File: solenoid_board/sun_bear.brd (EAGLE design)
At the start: 38.1 x 38.1 mm, 31 parts, among them Q1 MOSFET-NCHANNELSMD, Q2 MOSFET-NCHANNELSMD, Q3 MOSFET-NCHANNELSMD, Q4 MOSFET-NCHANNELSMD

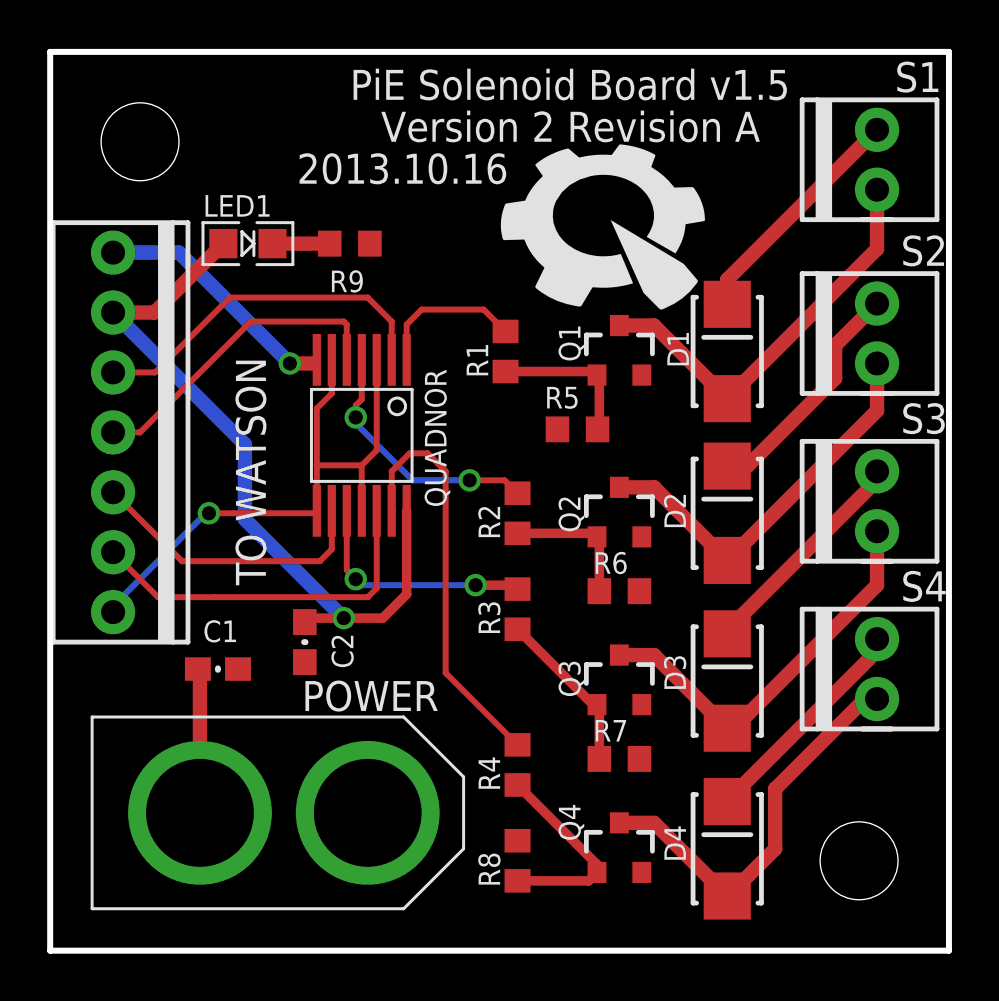
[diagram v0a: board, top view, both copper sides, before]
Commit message: Fixed Right Angle Traces on Sunbear
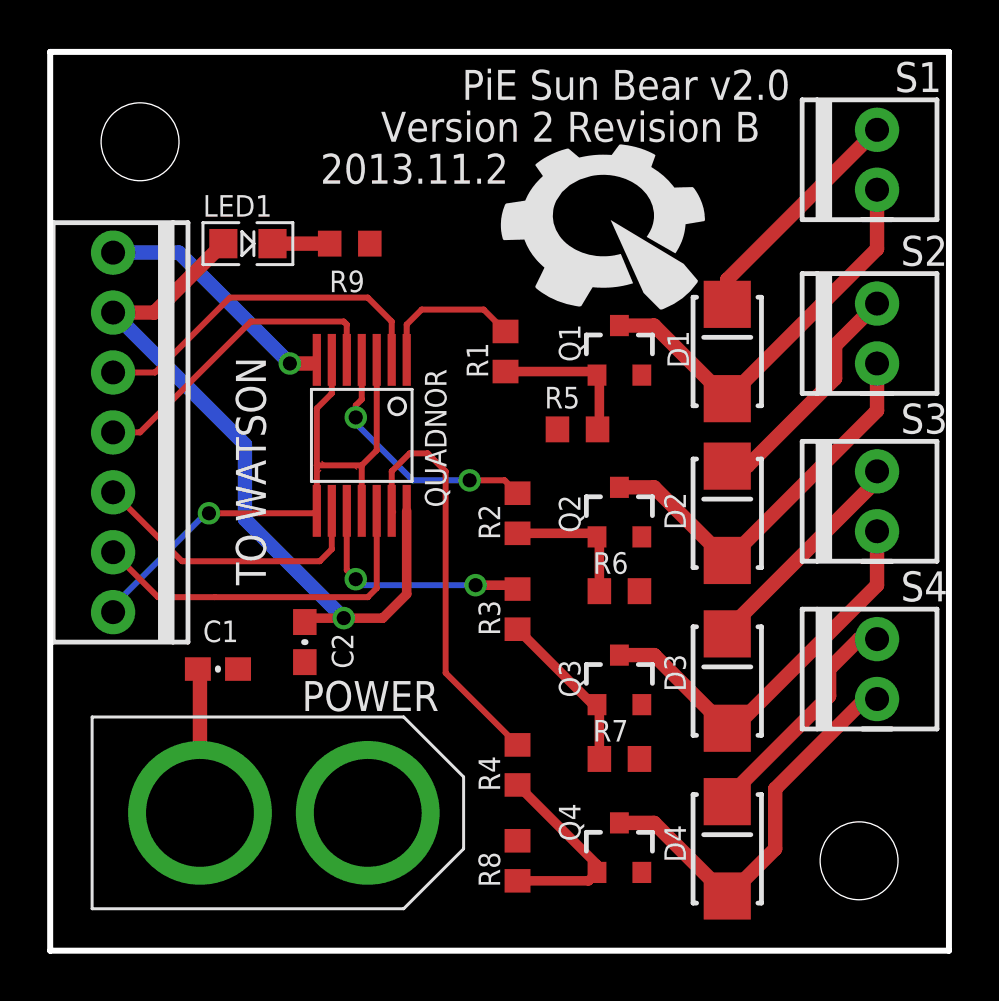
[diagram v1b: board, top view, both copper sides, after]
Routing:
- added copper zone on layer 1, net IO61
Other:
- board text added: "2013.11.2"
- board text added: "PiE Sun Bear v2.0"
- board text added: "Version 2 Revision B"
- board text removed: "2013.10.16"
- board text removed: "PiE Solenoid Board v1.5"
- board text removed: "Version 2 Revision A"
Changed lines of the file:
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@@
 <wire x1="38.1" y1="38.1" x2="0" y2="38.1" width="0.254" layer="20"/>
 <wire x1="0" y1="38.1" x2="0" y2="0" width="0.254" layer="20"/>
-<text x="31.369" y="37.338" size="1.27" layer="25" font="vector" ratio="20" rot="R180">PiE Solenoid Board v1.5</text>
-<text x="30.099" y="35.56" size="1.27" layer="21" font="vector" ratio="20" rot="R180">Version 2 Revision A</text>
-<text x="19.431" y="33.782" size="1.27" layer="21" font="vector" ratio="20" rot="R180">2013.10.16</text>
+<text x="31.369" y="37.338" size="1.27" layer="25" font="vector" ratio="20" rot="R180">PiE Sun Bear v2.0</text>
+<text x="30.099" y="35.56" size="1.27" layer="21" font="vector" ratio="20" rot="R180">Version 2 Revision B</text>
+<text x="19.431" y="33.782" size="1.27" layer="21" font="vector" ratio="20" rot="R180">2013.11.2</text>
 <text x="10.668" y="10.16" size="1.27" layer="21" font="vector" ratio="20">POWER</text>
 <text x="9.144" y="15.494" size="1.27" layer="21" font="vector" ratio="20" rot="SR90">TO WATSON</text>
@@
 <wire x1="34.798" y1="19.685" x2="34.798" y2="20.066" width="0.6096" layer="1"/>
 <wire x1="34.798" y1="20.066" x2="35.052" y2="20.32" width="0.6096" layer="1"/>
-<wire x1="28.702" y1="6.318" x2="28.702" y2="6.35" width="0.6096" layer="1"/>
-<wire x1="28.702" y1="6.35" x2="35.052" y2="12.7" width="0.6096" layer="1"/>
-<wire x1="35.052" y1="12.7" x2="35.052" y2="13.208" width="0.6096" layer="1"/>
-<wire x1="33.274" y1="25.654" x2="28.702" y2="27.4" width="0" layer="19" extent="1-1"/>
-<wire x1="35.052" y1="20.32" x2="33.274" y2="24.257" width="0" layer="19" extent="1-1"/>
-<wire x1="35.052" y1="13.208" x2="28.702" y2="13.43" width="0" layer="19" extent="1-1"/>
-<wire x1="6.35" y1="5.842" x2="28.702" y2="6.318" width="0" layer="19" extent="1-1"/>
+<wire x1="28.702" y1="6.318" x2="28.702" y2="6.477" width="0.6096" layer="1"/>
+<wire x1="28.702" y1="6.477" x2="33.02" y2="10.795" width="0.6096" layer="1"/>
+<wire x1="33.02" y1="10.795" x2="33.02" y2="11.938" width="0.6096" layer="1"/>
+<wire x1="33.02" y1="11.938" x2="34.29" y2="13.208" width="0.6096" layer="1"/>
+<wire x1="34.29" y1="13.208" x2="35.052" y2="13.208" width="0.6096" layer="1"/>
 </signal>
 <signal name="N$15">
@@
 <wire x1="11.303" y1="20.574" x2="11.303" y2="18.644" width="0.254" layer="1"/>
 <wire x1="11.938" y1="25.044" x2="11.938" y2="23.622" width="0.254" layer="1"/>
-<wire x1="13.208" y1="20.574" x2="11.303" y2="20.574" width="0.254" layer="1"/>
-<wire x1="13.208" y1="20.574" x2="13.843" y2="21.209" width="0.254" layer="1"/>
 <wire x1="13.843" y1="21.209" x2="13.843" y2="25.044" width="0.254" layer="1"/>
 <contactref element="WATSON" pad="7"/>
 <wire x1="6.604" y1="18.542" x2="2.667" y2="14.605" width="0.254" layer="16"/>
 <wire x1="2.667" y1="14.605" x2="2.667" y2="14.351" width="0.254" layer="16"/>
+<wire x1="13.208" y1="20.574" x2="13.843" y2="21.209" width="0.254" layer="1"/>
+<wire x1="11.303" y1="20.574" x2="13.208" y2="20.574" width="0.254" layer="1"/>
+<polygon width="0.254" layer="1">
+<vertex x="13.208" y="20.574"/>
+<vertex x="12.827" y="20.574"/>
+<vertex x="13.208" y="20.193"/>
+</polygon>
+<polygon width="0.254" layer="1">
+<vertex x="11.303" y="20.193"/>
+<vertex x="11.684" y="20.574"/>
+<vertex x="11.303" y="20.955"/>
+</polygon>
 </signal>
 <signal name="VCC" class="1">
@@
 </signal>
 </signals>
+<errors>
+</errors>
 </board>
 </drawing>

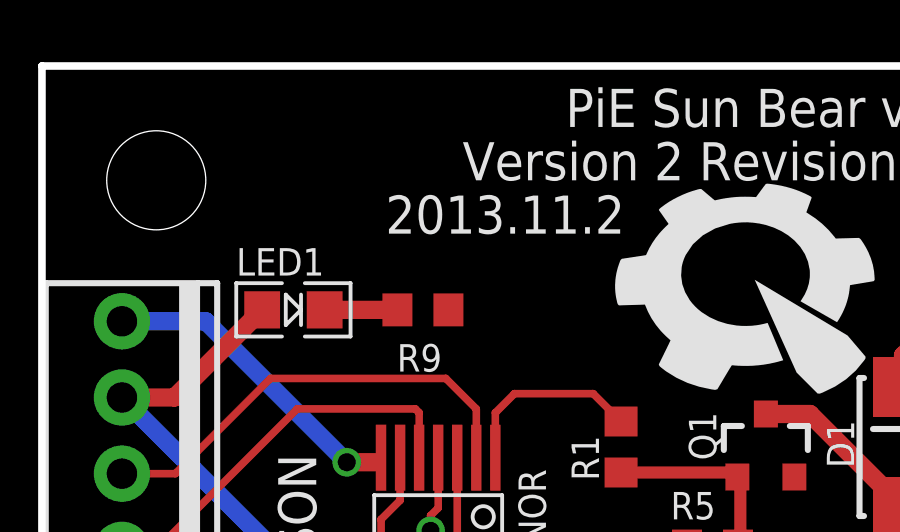
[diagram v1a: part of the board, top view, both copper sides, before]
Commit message: Silkscreen date changed to 11/11
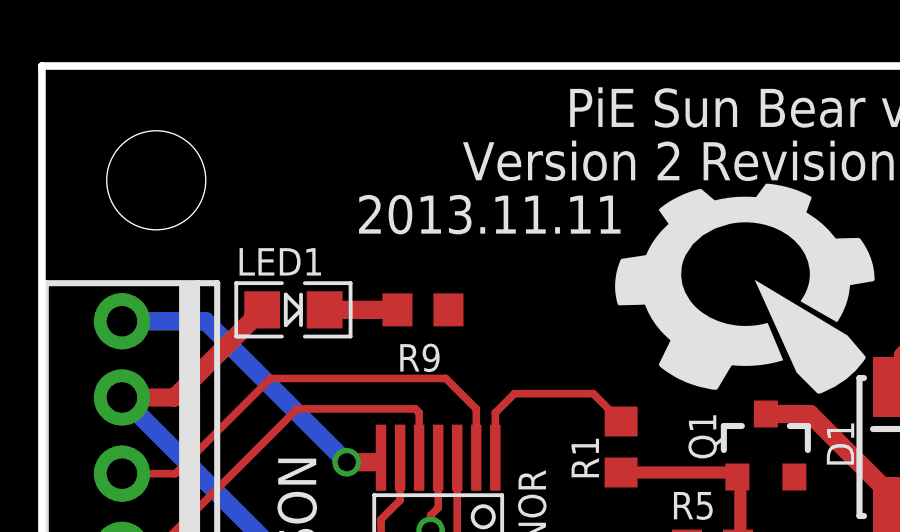
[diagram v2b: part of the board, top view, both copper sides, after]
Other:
- board text added: "2013.11.11"
- board text removed: "2013.11.2"
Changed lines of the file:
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@@
 <text x="31.369" y="37.338" size="1.27" layer="25" font="vector" ratio="20" rot="R180">PiE Sun Bear v2.0</text>
 <text x="30.099" y="35.56" size="1.27" layer="21" font="vector" ratio="20" rot="R180">Version 2 Revision B</text>
-<text x="19.431" y="33.782" size="1.27" layer="21" font="vector" ratio="20" rot="R180">2013.11.2</text>
+<text x="19.431" y="33.782" size="1.27" layer="21" font="vector" ratio="20" rot="R180">2013.11.11</text>
 <text x="10.668" y="10.16" size="1.27" layer="21" font="vector" ratio="20">POWER</text>
 <text x="9.144" y="15.494" size="1.27" layer="21" font="vector" ratio="20" rot="SR90">TO WATSON</text>

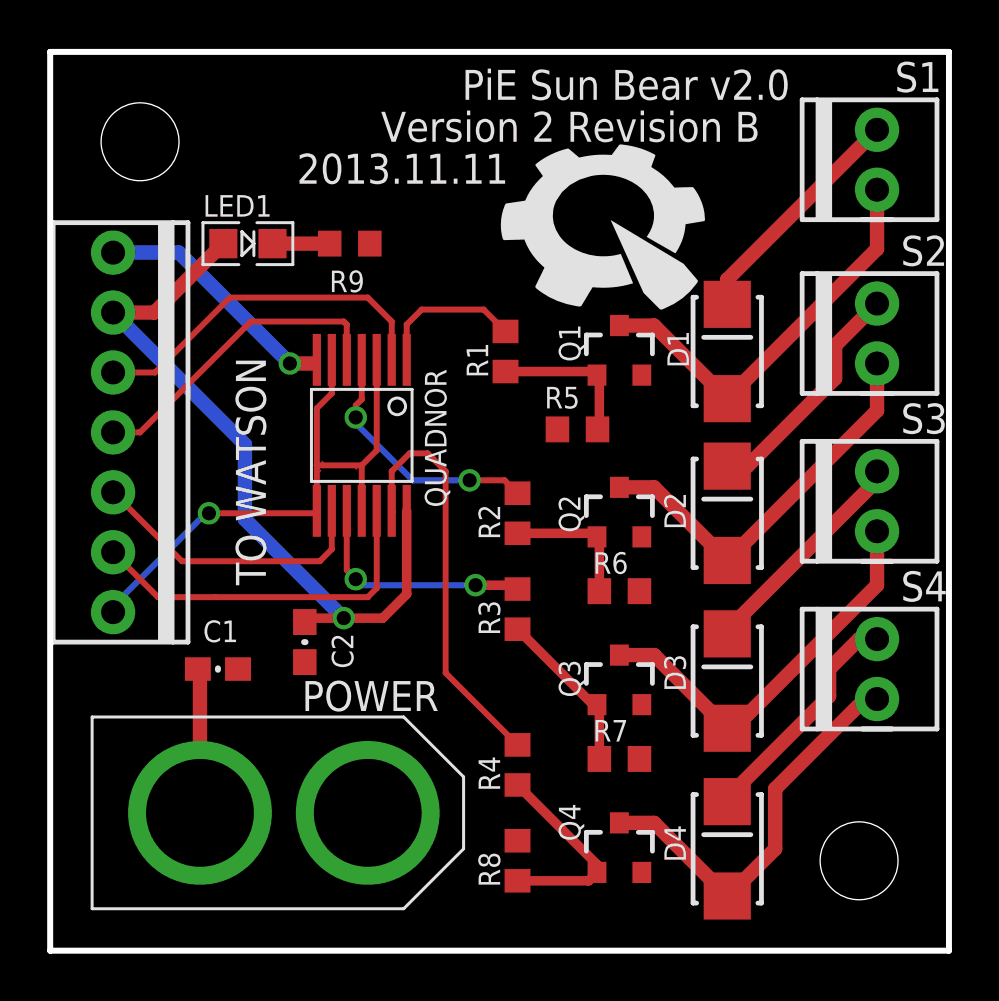
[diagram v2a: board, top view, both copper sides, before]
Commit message: Moved connectors, added screw hole for enclosure
Moved the XT60 and M70 a little bit down to give the connectors some
extra clearance, added a third screw hole to get three points of
contact, moved the silkscreen PiE logo a bit.
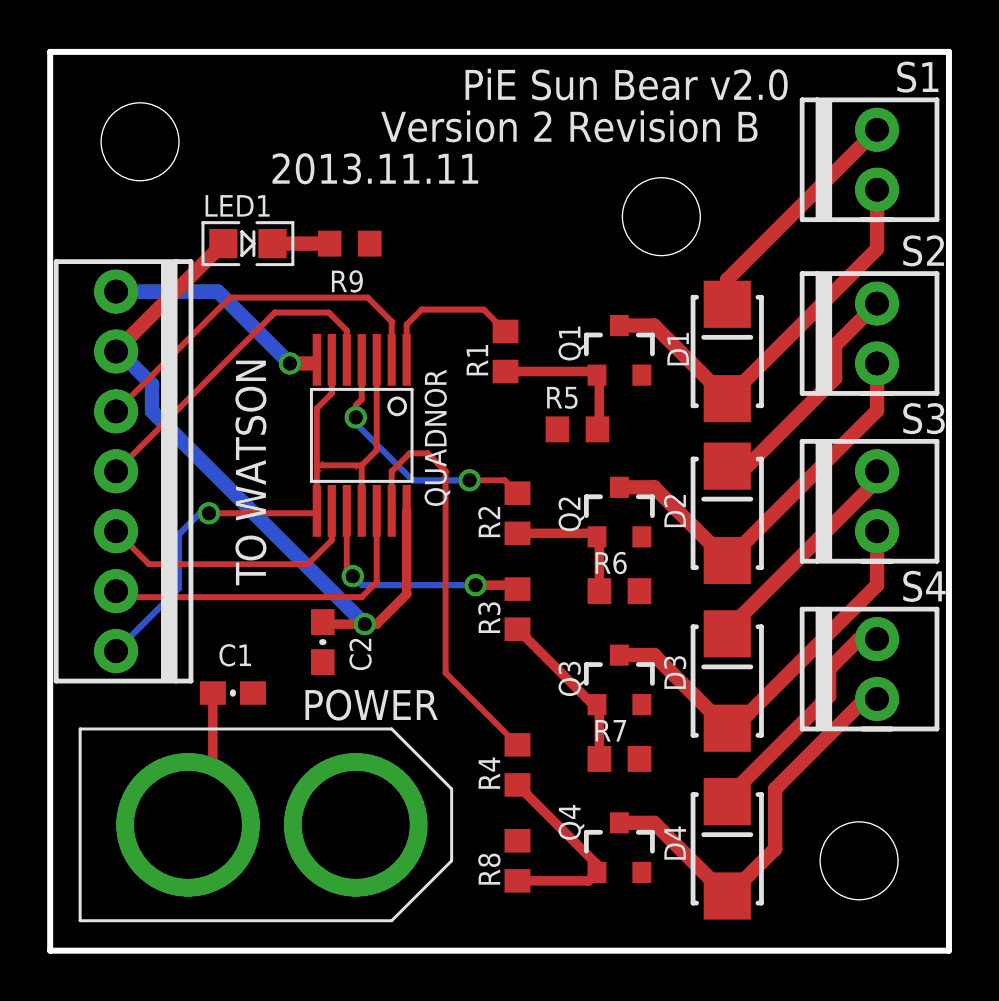
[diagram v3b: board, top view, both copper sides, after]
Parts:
- added U$6: Mounting + Test, pie:STAND-OFF
- moved U$1 26.3 mm to (27.3, 4.95), flipped to the bottom
- moved WATSON 1.66 mm to (2.79, 20.3)
- moved C1 1.20 mm to (7.75, 10.9)
- moved C2 0.76 mm to (11.6, 13.1)
- moved U$2 0.72 mm to (9.40, 5.33)
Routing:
- net IO61: track 25.8 -> 27.5 mm
- net VCC: track 31.2 -> 30.1 mm
- net IO65: track 15.4 -> 14.4 mm
- net IO21: track 12.3 -> 11.4 mm
- net GND: track 10.6 -> 9.83 mm
- net IO63: track 13.4 -> 14.1 mm
- net IO64: track 15.2 -> 15.7 mm
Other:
- board text added: "Copyright (c) 2013, Pioneers in Engineering All rights reserved. Design by: Sumita Ghosh, Sahar Mesri, Rhett Gentile, and Krystyn Neisess. This design is open source hardware. For more information visit pioneers.berkeley.edu/ opensource"
- board text removed: "Copyright (c) 2013, Pioneers in Engineering All rights reserved. Design by: Sumita Ghosh, Sahar Mesri, Rhett Gentile, and Krystyn Neisess. This design is open source hardware. For more information, visit pioneers.berkeley.edu/ opensource"

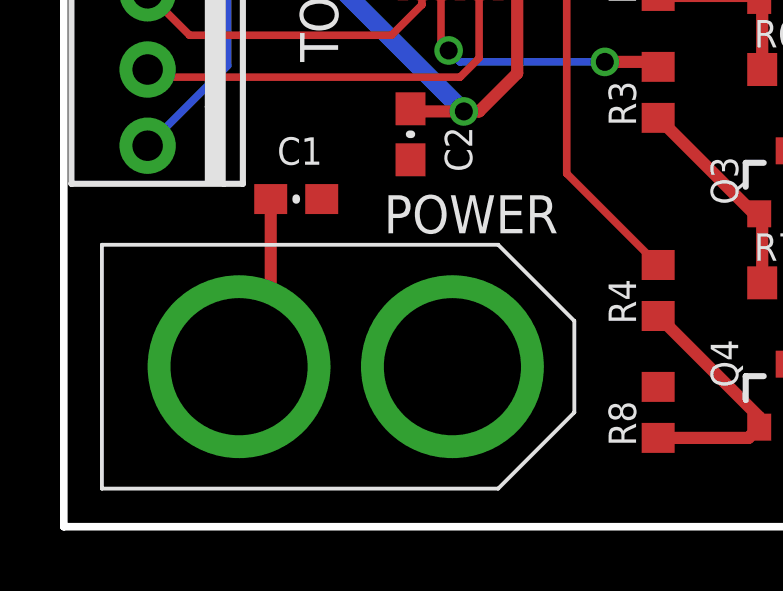
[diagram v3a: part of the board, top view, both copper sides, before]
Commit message: Added Andersons
Also deleted sherlock_anderson because it's outdated and redundant (uses
last year's Sherlock).
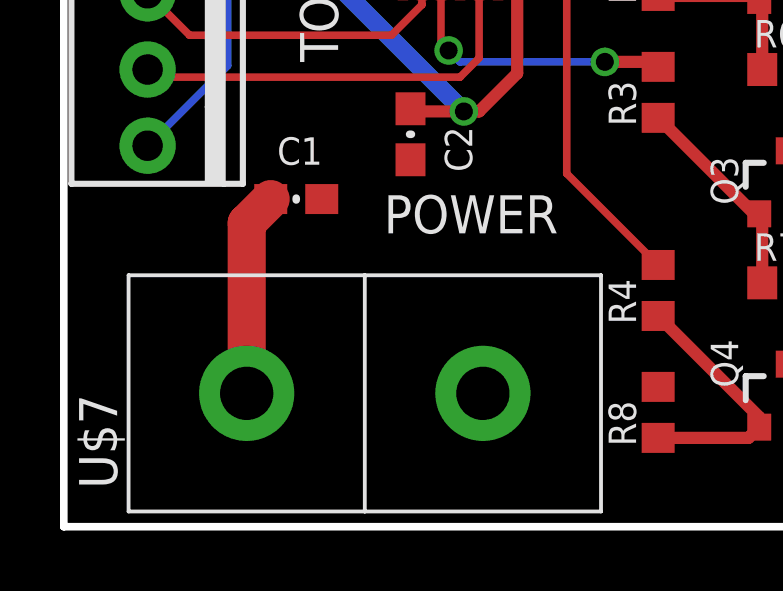
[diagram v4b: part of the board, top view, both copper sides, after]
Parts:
- removed U$2: XT60CONNECTOR, pie:XT60CONNECTOR
- added U$7: ANDERSONVERTICAL, pie:ANDERSON_VERTICAL
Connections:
- net 12V: now also U$7.PIN2; no longer U$2.12V
- net GND: now also U$7.PIN1; no longer U$2.GND
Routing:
- net 12V: track 46.1 -> 46.9 mm
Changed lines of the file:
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@@
 <layer number="97" name="Info" color="7" fill="1" visible="no" active="no"/>
 <layer number="98" name="Guide" color="6" fill="1" visible="no" active="no"/>
+<layer number="99" name="SpiceOrder" color="5" fill="1" visible="no" active="no"/>
 <layer number="100" name="ISO" color="7" fill="1" visible="yes" active="yes"/>
 <layer number="101" name="Design Layout" color="10" fill="1" visible="no" active="no"/>
@@
 </element>
 <element name="U$1" library="pie" package="PIE-LOGO-SMALL" value="" x="27.305" y="4.953" rot="MR0"/>
-<element name="U$2" library="pie" package="XT60CONNECTOR" value="XT60CONNECTOR" x="9.398" y="5.334">
-<attribute name="PARTNUMBER" value="PRT-10474 " x="9.398" y="5.334" size="1.778" layer="27" display="off"/>
-</element>
 <element name="S1" library="pie" package="1X02-MTA" value="" x="35.052" y="33.528" smashed="yes" rot="R90">
 <attribute name="NAME" x="37.7952" y="37.6682" size="1.27" layer="25" font="vector" ratio="20" rot="R180"/>
@@
 </element>
 <element name="U$6" library="pie" package="STAND-OFF" value="Mounting + Test" x="25.908" y="31.115"/>
+<element name="U$7" library="pie" package="ANDERSON_VERTICAL" value="ANDERSONVERTICAL" x="10.033" y="4.445" rot="R90">
+<attribute name="PARTNUMBER" value="1377G3" x="10.033" y="4.445" size="1.778" layer="27" rot="R90" display="off"/>
+</element>
 </elements>
 <signals>
@@
 <vertex x="0" y="0"/>
 </polygon>
-<contactref element="U$2" pad="12V"/>
 <contactref element="C1" pad="1"/>
 <contactref element="D2" pad="C"/>
@@
 <wire x1="33.02" y1="11.938" x2="34.29" y2="13.208" width="0.6096" layer="1"/>
 <wire x1="34.29" y1="13.208" x2="35.052" y2="13.208" width="0.6096" layer="1"/>
-<wire x1="6.897" y1="10.922" x2="6.897" y2="6.389" width="0.4064" layer="1"/>
-<wire x1="6.897" y1="6.389" x2="5.842" y2="5.334" width="0.4064" layer="1"/>
+<contactref element="U$7" pad="PIN2"/>
+<wire x1="6.897" y1="10.922" x2="6.096" y2="10.121" width="1.27" layer="1"/>
+<wire x1="6.096" y1="10.121" x2="6.096" y2="4.445" width="1.27" layer="1"/>
 </signal>
 <signal name="N$15">
@@
 <contactref element="QUADNOR" pad="GND"/>
 <via x="10.16" y="24.892" extent="1-16" drill="0.6"/>
-<contactref element="U$2" pad="GND"/>
 <contactref element="C1" pad="2"/>
 <contactref element="Q1" pad="2"/>
@@
 <wire x1="2.794" y1="27.94" x2="7.112" y2="27.94" width="0.6096" layer="16"/>
 <wire x1="7.112" y1="27.94" x2="10.16" y2="24.892" width="0.6096" layer="16"/>
+<contactref element="U$7" pad="PIN1"/>
 </signal>
 <signal name="N$2">
